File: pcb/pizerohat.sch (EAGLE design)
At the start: 21 parts, among them J1 MF-CON-2.54mm-01x03, J2 MF-CON-2.54mm-01x06, J3 MF-CON-2.54mm-01x03, J4 MF-CON-2.54mm-01x06, J5 MF-CON-2.54mm-01x03, J6 MF-CON-2.54mm-01x03, U1 MAX14778ETP+, U2 MAX3089CSD+, U3 MF-DSC-SOT233-BSS84

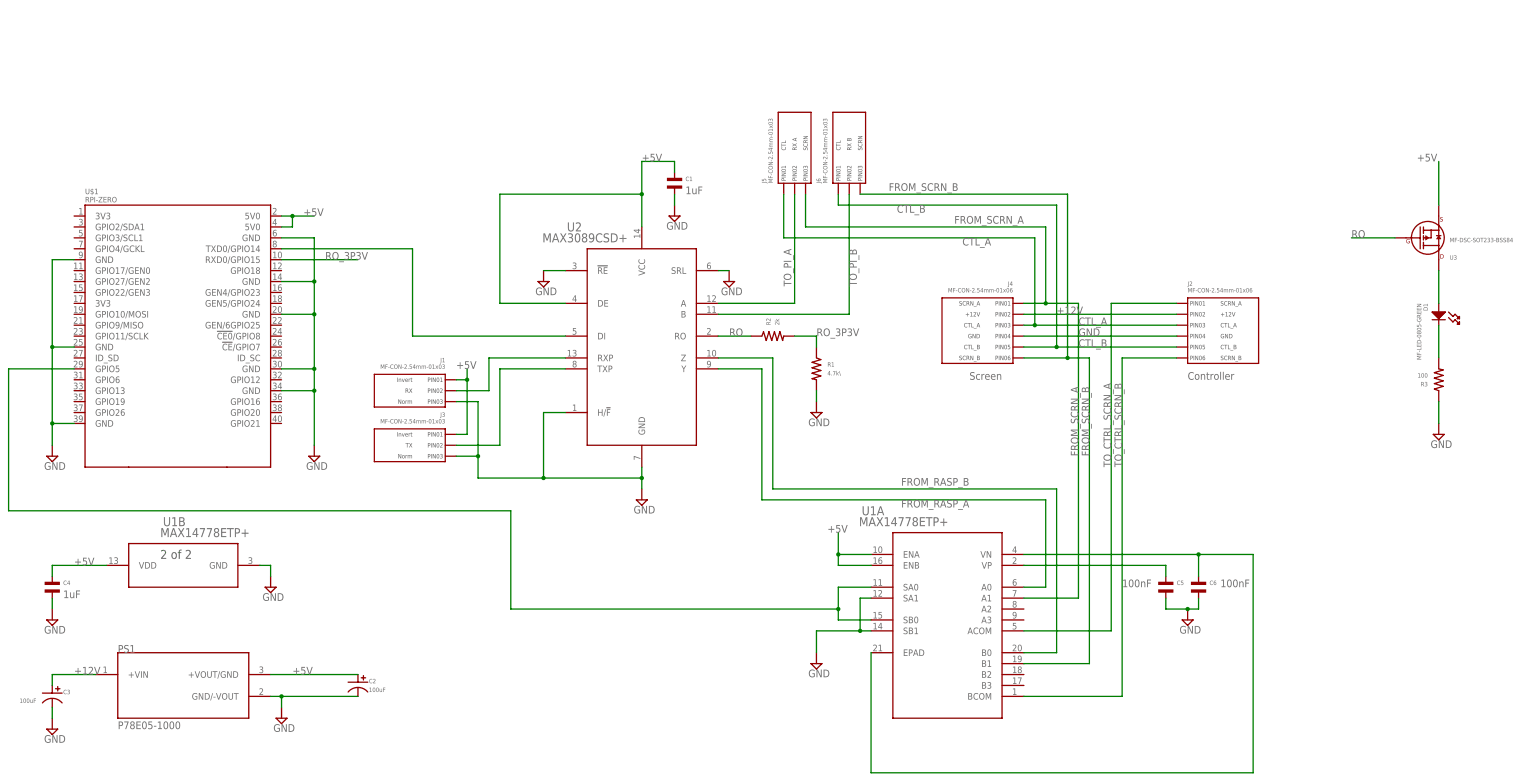
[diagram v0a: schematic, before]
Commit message: Rordered mux pins, added pulldown for default muxsel
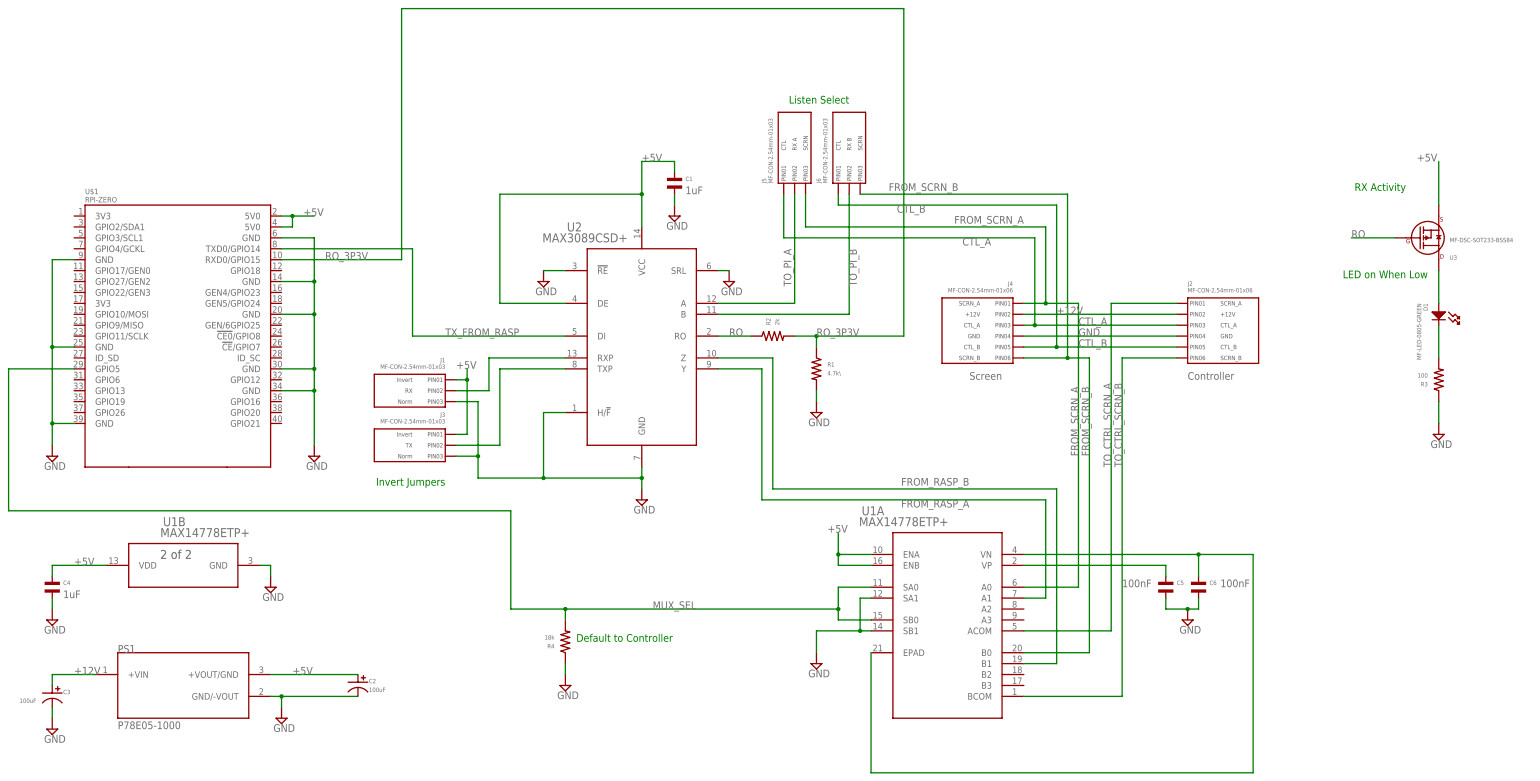
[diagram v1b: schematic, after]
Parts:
- added R4: 18k, MF_Passives:RESISTOR_0603
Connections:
- net N$2 renamed TX_FROM_RASP
- removed net N$8: U$1.GPIO5, U1A.SA0, U1A.SB0
- new net MUX_SEL: R4.P$2, U$1.GPIO5, U1A.SA0, U1A.SB0
- net FROM_RASP_A: now also U1A.A1; no longer U1A.A0
- net FROM_RASP_B: now also U1A.B1; no longer U1A.B0
- net FROM_SCRN_A: now also U1A.A0; no longer U1A.A1
- net FROM_SCRN_B: now also U1A.B0; no longer U1A.B1
- net GND: now also R4.P$1
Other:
- note added: "Default to Controller"
- note added: "Invert Jumpers"
- note added: "LED on When Low"
- note added: "Listen Select"
- note added: "RX Activity"
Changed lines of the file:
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@@
 <attribute name="LABEL" value="RX"/>
 </part>
+<part name="R4" library="MF_Passives" deviceset="RESISTOR" device="_0603" value="18k">
+<attribute name="HOUSEPART" value="YES"/>
+<attribute name="MPN" value="MF-RES-0603-18K"/>
+</part>
+<part name="SUPPLY15" library="supply2" library_urn="urn:adsk.eagle:library:372" deviceset="GND" device=""/>
 </parts>
 <sheets>
 <sheet>
 <plain>
+<text x="185.42" y="35.56" size="1.778" layer="91">Default to Controller</text>
+<text x="378.46" y="142.24" size="1.778" layer="91" rot="R180">RX Activity</text>
+<text x="383.54" y="121.92" size="1.778" layer="91" rot="R180">LED on When Low</text>
+<text x="154.94" y="73.66" size="1.778" layer="91" rot="R180">Invert Jumpers</text>
+<text x="248.92" y="162.56" size="1.778" layer="91" rot="R180">Listen Select</text>
 </plain>
 <instances>
@@
 <attribute name="VALUE" x="388.62" y="129.54" size="1.016" layer="96" font="vector" rot="MR180"/>
 <attribute name="LABEL" x="383.54" y="129.54" size="1.778" layer="96" rot="MR180" display="off"/>
+</instance>
+<instance part="R4" gate="G$1" x="182.88" y="35.56" smashed="yes" rot="R180">
+<attribute name="NAME" x="180.34" y="34.036" size="1.016" layer="95" font="vector" rot="R180" align="top-left"/>
+<attribute name="VALUE" x="180.34" y="37.084" size="1.016" layer="96" font="vector" rot="R180"/>
+</instance>
+<instance part="SUPPLY15" gate="GND" x="182.88" y="25.4" smashed="yes">
+<attribute name="VALUE" x="180.975" y="22.225" size="1.778" layer="96"/>
 </instance>
 </instances>
@@
 <wire x1="386.08" y1="86.36" x2="386.08" y2="91.44" width="0.1524" layer="91"/>
 </segment>
+<segment>
+<pinref part="R4" gate="G$1" pin="P$1"/>
+<pinref part="SUPPLY15" gate="GND" pin="GND"/>
+<wire x1="182.88" y1="30.48" x2="182.88" y2="27.94" width="0.1524" layer="91"/>
+</segment>
 </net>
 <net name="+12V" class="0">
@@
 <net name="RO_3P3V" class="0">
 <segment>
+<pinref part="U$1" gate="G$1" pin="RXD0/GPIO15"/>
+<wire x1="116.84" y1="124.46" x2="144.78" y2="124.46" width="0.1524" layer="91"/>
+<label x="127" y="124.46" size="1.778" layer="95"/>
+<wire x1="144.78" y1="124.46" x2="144.78" y2="182.88" width="0.1524" layer="91"/>
+<wire x1="144.78" y1="182.88" x2="261.62" y2="182.88" width="0.1524" layer="91"/>
+<wire x1="261.62" y1="182.88" x2="261.62" y2="106.68" width="0.1524" layer="91"/>
 <pinref part="R2" gate="G$1" pin="P$2"/>
 <wire x1="236.22" y1="106.68" x2="241.3" y2="106.68" width="0.1524" layer="91"/>
@@
 <wire x1="241.3" y1="106.68" x2="241.3" y2="104.14" width="0.1524" layer="91"/>
 <label x="241.3" y="106.68" size="1.778" layer="95"/>
-</segment>
-<segment>
-<pinref part="U$1" gate="G$1" pin="RXD0/GPIO15"/>
-<wire x1="116.84" y1="124.46" x2="134.62" y2="124.46" width="0.1524" layer="91"/>
-<label x="127" y="124.46" size="1.778" layer="95"/>
-</segment>
-</net>
-<net name="N$2" class="0">
+<wire x1="261.62" y1="106.68" x2="241.3" y2="106.68" width="0.1524" layer="91"/>
+<junction x="241.3" y="106.68"/>
+</segment>
+</net>
+<net name="TX_FROM_RASP" class="0">
 <segment>
 <pinref part="U$1" gate="G$1" pin="TXD0/GPIO14"/>
@@
 <pinref part="U2" gate="A" pin="DI"/>
 <wire x1="147.32" y1="106.68" x2="182.88" y2="106.68" width="0.1524" layer="91"/>
+<label x="154.94" y="106.68" size="1.778" layer="95"/>
 </segment>
 </net>
@@
 <wire x1="294.64" y1="114.3" x2="302.26" y2="114.3" width="0.1524" layer="91"/>
 <junction x="294.64" y="114.3"/>
-<wire x1="302.26" y1="114.3" x2="302.26" y2="45.72" width="0.1524" layer="91"/>
-<pinref part="U1" gate="A" pin="A1"/>
-<wire x1="302.26" y1="45.72" x2="289.56" y2="45.72" width="0.1524" layer="91"/>
+<wire x1="302.26" y1="114.3" x2="302.26" y2="48.26" width="0.1524" layer="91"/>
 <label x="302.26" y="78.74" size="1.778" layer="95" rot="R90"/>
 <label x="289.56" y="134.62" size="1.778" layer="95" rot="R180"/>
+<pinref part="U1" gate="A" pin="A0"/>
+<wire x1="289.56" y1="48.26" x2="302.26" y2="48.26" width="0.1524" layer="91"/>
 </segment>
 </net>
@@
 <wire x1="251.46" y1="139.7" x2="299.72" y2="139.7" width="0.1524" layer="91"/>
 <wire x1="299.72" y1="139.7" x2="299.72" y2="101.6" width="0.1524" layer="91"/>
-<pinref part="U1" gate="A" pin="B1"/>
-<wire x1="289.56" y1="30.48" x2="304.8" y2="30.48" width="0.1524" layer="91"/>
-<wire x1="304.8" y1="30.48" x2="304.8" y2="101.6" width="0.1524" layer="91"/>
+<wire x1="304.8" y1="33.02" x2="304.8" y2="101.6" width="0.1524" layer="91"/>
 <wire x1="304.8" y1="101.6" x2="299.72" y2="101.6" width="0.1524" layer="91"/>
 <junction x="299.72" y="101.6"/>
 <label x="304.8" y="78.74" size="1.778" layer="95" rot="R90"/>
 <label x="274.32" y="142.24" size="1.778" layer="95" rot="R180"/>
+<pinref part="U1" gate="A" pin="B0"/>
+<wire x1="289.56" y1="33.02" x2="304.8" y2="33.02" width="0.1524" layer="91"/>
 </segment>
 </net>
@@
 </segment>
 </net>
-<net name="N$8" class="0">
+<net name="MUX_SEL" class="0">
 <segment>
 <pinref part="U1" gate="A" pin="SB0"/>
@@
 <wire x1="53.34" y1="66.04" x2="170.18" y2="66.04" width="0.1524" layer="91"/>
 <wire x1="170.18" y1="66.04" x2="170.18" y2="43.18" width="0.1524" layer="91"/>
-<wire x1="170.18" y1="43.18" x2="246.38" y2="43.18" width="0.1524" layer="91"/>
+<wire x1="170.18" y1="43.18" x2="182.88" y2="43.18" width="0.1524" layer="91"/>
 <junction x="246.38" y="43.18"/>
+<pinref part="R4" gate="G$1" pin="P$2"/>
+<wire x1="182.88" y1="43.18" x2="246.38" y2="43.18" width="0.1524" layer="91"/>
+<wire x1="182.88" y1="40.64" x2="182.88" y2="43.18" width="0.1524" layer="91"/>
+<junction x="182.88" y="43.18"/>
+<label x="203.2" y="43.18" size="1.778" layer="95"/>
 </segment>
 </net>
@@
 <wire x1="228.6" y1="99.06" x2="228.6" y2="68.58" width="0.1524" layer="91"/>
 <wire x1="228.6" y1="68.58" x2="294.64" y2="68.58" width="0.1524" layer="91"/>
-<wire x1="294.64" y1="68.58" x2="294.64" y2="48.26" width="0.1524" layer="91"/>
-<pinref part="U1" gate="A" pin="A0"/>
-<wire x1="294.64" y1="48.26" x2="289.56" y2="48.26" width="0.1524" layer="91"/>
+<wire x1="294.64" y1="68.58" x2="294.64" y2="45.72" width="0.1524" layer="91"/>
 <label x="276.86" y="68.58" size="1.778" layer="95" rot="R180"/>
+<pinref part="U1" gate="A" pin="A1"/>
+<wire x1="294.64" y1="45.72" x2="289.56" y2="45.72" width="0.1524" layer="91"/>
 </segment>
 </net>
@@
 <wire x1="231.14" y1="101.6" x2="231.14" y2="71.12" width="0.1524" layer="91"/>
 <wire x1="231.14" y1="71.12" x2="297.18" y2="71.12" width="0.1524" layer="91"/>
-<wire x1="297.18" y1="71.12" x2="297.18" y2="33.02" width="0.1524" layer="91"/>
-<pinref part="U1" gate="A" pin="B0"/>
-<wire x1="297.18" y1="33.02" x2="289.56" y2="33.02" width="0.1524" layer="91"/>
+<wire x1="297.18" y1="71.12" x2="297.18" y2="30.48" width="0.1524" layer="91"/>
 <label x="276.86" y="73.66" size="1.778" layer="95" rot="R180"/>
-</segment>
-</net>
+<pinref part="U1" gate="A" pin="B1"/>
+<wire x1="297.18" y1="30.48" x2="289.56" y2="30.48" width="0.1524" layer="91"/>
+</segment>
+</net>

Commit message: Power TX down when not in use
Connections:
- net +5V: no longer U2.DE
- net MUX_SEL: now also U2.DE
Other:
- note added: "Default is Passthrough Mode"
- note added: "High = Inject"
- note added: "Low = Passthrough"
- note added: "Power Off TX When not used"
- note removed: "Default to Controller"
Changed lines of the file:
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@@
 <sheet>
 <plain>
-<text x="185.42" y="35.56" size="1.778" layer="91">Default to Controller</text>
+<text x="185.42" y="35.56" size="1.778" layer="91">Default is Passthrough Mode</text>
 <text x="378.46" y="142.24" size="1.778" layer="91" rot="R180">RX Activity</text>
 <text x="383.54" y="121.92" size="1.778" layer="91" rot="R180">LED on When Low</text>
 <text x="154.94" y="73.66" size="1.778" layer="91" rot="R180">Invert Jumpers</text>
 <text x="248.92" y="162.56" size="1.778" layer="91" rot="R180">Listen Select</text>
+<text x="154.94" y="60.96" size="1.778" layer="91">High = Inject</text>
+<text x="147.32" y="55.88" size="1.778" layer="91">Low = Passthrough</text>
+<text x="152.4" y="111.76" size="1.778" layer="91">Power Off TX When not used</text>
 </plain>
 <instances>
@@
 </segment>
 <segment>
-<pinref part="U2" gate="A" pin="VCC"/>
-<label x="200.66" y="147.32" size="1.778" layer="95"/>
-<wire x1="200.66" y1="132.08" x2="200.66" y2="139.7" width="0.1524" layer="91"/>
-<wire x1="200.66" y1="139.7" x2="200.66" y2="147.32" width="0.1524" layer="91"/>
-<wire x1="200.66" y1="147.32" x2="208.28" y2="147.32" width="0.1524" layer="91"/>
-<pinref part="C1" gate="G$1" pin="P$1"/>
-<wire x1="208.28" y1="147.32" x2="208.28" y2="144.78" width="0.1524" layer="91"/>
-<pinref part="U2" gate="A" pin="DE"/>
-<wire x1="182.88" y1="114.3" x2="167.64" y2="114.3" width="0.1524" layer="91"/>
-<wire x1="167.64" y1="114.3" x2="167.64" y2="139.7" width="0.1524" layer="91"/>
-<wire x1="167.64" y1="139.7" x2="200.66" y2="139.7" width="0.1524" layer="91"/>
-<junction x="200.66" y="139.7"/>
-</segment>
-<segment>
 <pinref part="J3" gate="G$1" pin="PIN1"/>
 <wire x1="157.48" y1="83.82" x2="160.02" y2="83.82" width="0.1524" layer="91"/>
@@
 <wire x1="386.08" y1="137.16" x2="386.08" y2="147.32" width="0.1524" layer="91"/>
 <label x="381" y="147.32" size="1.778" layer="95"/>
+</segment>
+<segment>
+<pinref part="C1" gate="G$1" pin="P$1"/>
+<wire x1="208.28" y1="147.32" x2="208.28" y2="144.78" width="0.1524" layer="91"/>
+<wire x1="200.66" y1="147.32" x2="208.28" y2="147.32" width="0.1524" layer="91"/>
+<pinref part="U2" gate="A" pin="VCC"/>
+<wire x1="200.66" y1="132.08" x2="200.66" y2="147.32" width="0.1524" layer="91"/>
+<label x="200.66" y="147.32" size="1.778" layer="95"/>
 </segment>
 </net>
@@
 </segment>
 </net>
+<net name="FROM_RASP_A" class="0">
+<segment>
+<pinref part="U2" gate="A" pin="Y"/>
+<wire x1="218.44" y1="99.06" x2="228.6" y2="99.06" width="0.1524" layer="91"/>
+<wire x1="228.6" y1="99.06" x2="228.6" y2="68.58" width="0.1524" layer="91"/>
+<wire x1="228.6" y1="68.58" x2="294.64" y2="68.58" width="0.1524" layer="91"/>
+<wire x1="294.64" y1="68.58" x2="294.64" y2="45.72" width="0.1524" layer="91"/>
+<label x="276.86" y="68.58" size="1.778" layer="95" rot="R180"/>
+<pinref part="U1" gate="A" pin="A1"/>
+<wire x1="294.64" y1="45.72" x2="289.56" y2="45.72" width="0.1524" layer="91"/>
+</segment>
+</net>
+<net name="FROM_RASP_B" class="0">
+<segment>
+<pinref part="U2" gate="A" pin="Z"/>
+<wire x1="218.44" y1="101.6" x2="231.14" y2="101.6" width="0.1524" layer="91"/>
+<wire x1="231.14" y1="101.6" x2="231.14" y2="71.12" width="0.1524" layer="91"/>
+<wire x1="231.14" y1="71.12" x2="297.18" y2="71.12" width="0.1524" layer="91"/>
+<wire x1="297.18" y1="71.12" x2="297.18" y2="30.48" width="0.1524" layer="91"/>
+<label x="276.86" y="73.66" size="1.778" layer="95" rot="R180"/>
+<pinref part="U1" gate="A" pin="B1"/>
+<wire x1="297.18" y1="30.48" x2="289.56" y2="30.48" width="0.1524" layer="91"/>
+</segment>
+</net>
+<net name="N$6" class="0">
+<segment>
+<pinref part="R3" gate="G$1" pin="P$2"/>
+<pinref part="D1" gate="G$1" pin="CATHODE"/>
+<wire x1="386.08" y1="101.6" x2="386.08" y2="109.22" width="0.1524" layer="91"/>
+</segment>
+</net>
+<net name="N$9" class="0">
+<segment>
+<pinref part="D1" gate="G$1" pin="ANODE"/>
+<pinref part="U3" gate="G$1" pin="DRAIN"/>
+<wire x1="386.08" y1="114.3" x2="386.08" y2="121.92" width="0.1524" layer="91"/>
+</segment>
+</net>
 <net name="MUX_SEL" class="0">
 <segment>
+<pinref part="U2" gate="A" pin="DE"/>
 <pinref part="U1" gate="A" pin="SB0"/>
 <wire x1="254" y1="40.64" x2="246.38" y2="40.64" width="0.1524" layer="91"/>
@@
 <wire x1="68.58" y1="99.06" x2="53.34" y2="99.06" width="0.1524" layer="91"/>
 <wire x1="53.34" y1="99.06" x2="53.34" y2="66.04" width="0.1524" layer="91"/>
-<wire x1="53.34" y1="66.04" x2="170.18" y2="66.04" width="0.1524" layer="91"/>
+<wire x1="53.34" y1="66.04" x2="132.08" y2="66.04" width="0.1524" layer="91"/>
+<wire x1="132.08" y1="66.04" x2="170.18" y2="66.04" width="0.1524" layer="91"/>
 <wire x1="170.18" y1="66.04" x2="170.18" y2="43.18" width="0.1524" layer="91"/>
 <wire x1="170.18" y1="43.18" x2="182.88" y2="43.18" width="0.1524" layer="91"/>
@@
 <junction x="182.88" y="43.18"/>
 <label x="203.2" y="43.18" size="1.778" layer="95"/>
-</segment>
-</net>
-<net name="FROM_RASP_A" class="0">
-<segment>
-<pinref part="U2" gate="A" pin="Y"/>
-<wire x1="218.44" y1="99.06" x2="228.6" y2="99.06" width="0.1524" layer="91"/>
-<wire x1="228.6" y1="99.06" x2="228.6" y2="68.58" width="0.1524" layer="91"/>
-<wire x1="228.6" y1="68.58" x2="294.64" y2="68.58" width="0.1524" layer="91"/>
-<wire x1="294.64" y1="68.58" x2="294.64" y2="45.72" width="0.1524" layer="91"/>
-<label x="276.86" y="68.58" size="1.778" layer="95" rot="R180"/>
-<pinref part="U1" gate="A" pin="A1"/>
-<wire x1="294.64" y1="45.72" x2="289.56" y2="45.72" width="0.1524" layer="91"/>
-</segment>
-</net>
-<net name="FROM_RASP_B" class="0">
-<segment>
-<pinref part="U2" gate="A" pin="Z"/>
-<wire x1="218.44" y1="101.6" x2="231.14" y2="101.6" width="0.1524" layer="91"/>
-<wire x1="231.14" y1="101.6" x2="231.14" y2="71.12" width="0.1524" layer="91"/>
-<wire x1="231.14" y1="71.12" x2="297.18" y2="71.12" width="0.1524" layer="91"/>
-<wire x1="297.18" y1="71.12" x2="297.18" y2="30.48" width="0.1524" layer="91"/>
-<label x="276.86" y="73.66" size="1.778" layer="95" rot="R180"/>
-<pinref part="U1" gate="A" pin="B1"/>
-<wire x1="297.18" y1="30.48" x2="289.56" y2="30.48" width="0.1524" layer="91"/>
-</segment>
-</net>
-<net name="N$6" class="0">
-<segment>
-<pinref part="R3" gate="G$1" pin="P$2"/>
-<pinref part="D1" gate="G$1" pin="CATHODE"/>
-<wire x1="386.08" y1="101.6" x2="386.08" y2="109.22" width="0.1524" layer="91"/>
-</segment>
-</net>
-<net name="N$9" class="0">
-<segment>
-<pinref part="D1" gate="G$1" pin="ANODE"/>
-<pinref part="U3" gate="G$1" pin="DRAIN"/>
-<wire x1="386.08" y1="114.3" x2="386.08" y2="121.92" width="0.1524" layer="91"/>
-</segment>
-</net>
+<wire x1="182.88" y1="114.3" x2="132.08" y2="114.3" width="0.1524" layer="91"/>
+<wire x1="132.08" y1="114.3" x2="132.08" y2="66.04" width="0.1524" layer="91"/>
+<junction x="132.08" y="66.04"/>
+<label x="162.56" y="114.3" size="1.778" layer="95"/>
+</segment>
+</net>
